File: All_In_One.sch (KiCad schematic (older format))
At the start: 106 parts, among them J1 MS_jumper_xaxis, J10 Motors, J11 Fan, J2 MS_jumper_yaxis, J3 Base_Proxy, J4 Water_Pump, J5 MS_jumper, J6 Stepper_xaxis, J7 Stepper_yaxis, J8 Arm_Proxy, J9 bluetooth, Q1 BC547, U1 Prashant_library_Arduino_Mega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, U10 PC817, U11 PC817, U12 PC817, U13 PC817, U14 5V_Regulator, U15 PC817, U16 PC817, U17 PC817, U2 L298, U3 L298, U4 5V_Regulator, U5 PC817, U6 PC817, U7 PC817, U8 PC817, U9 PC817

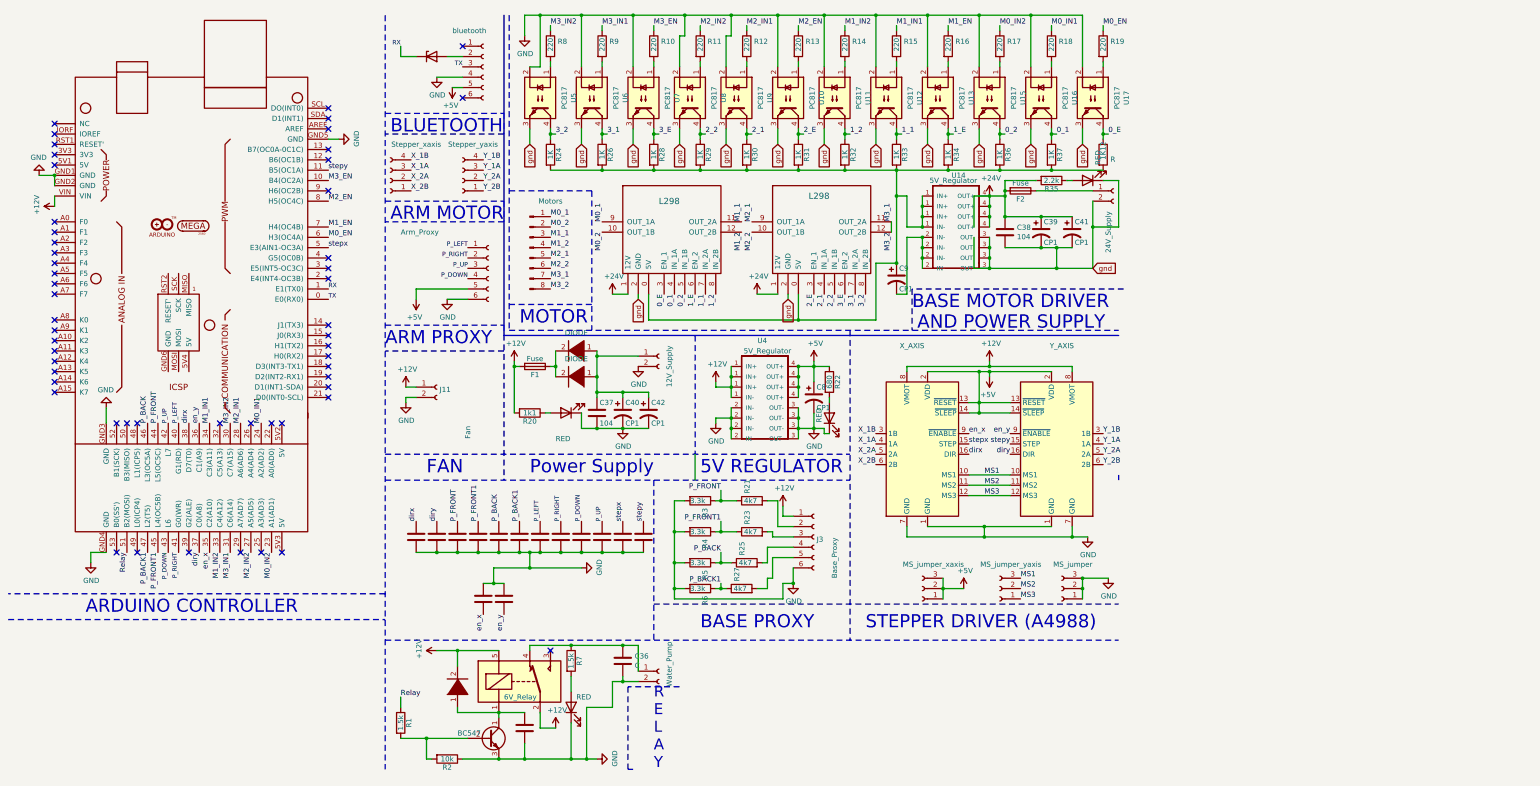
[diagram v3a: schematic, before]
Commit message: completed joining tracks!
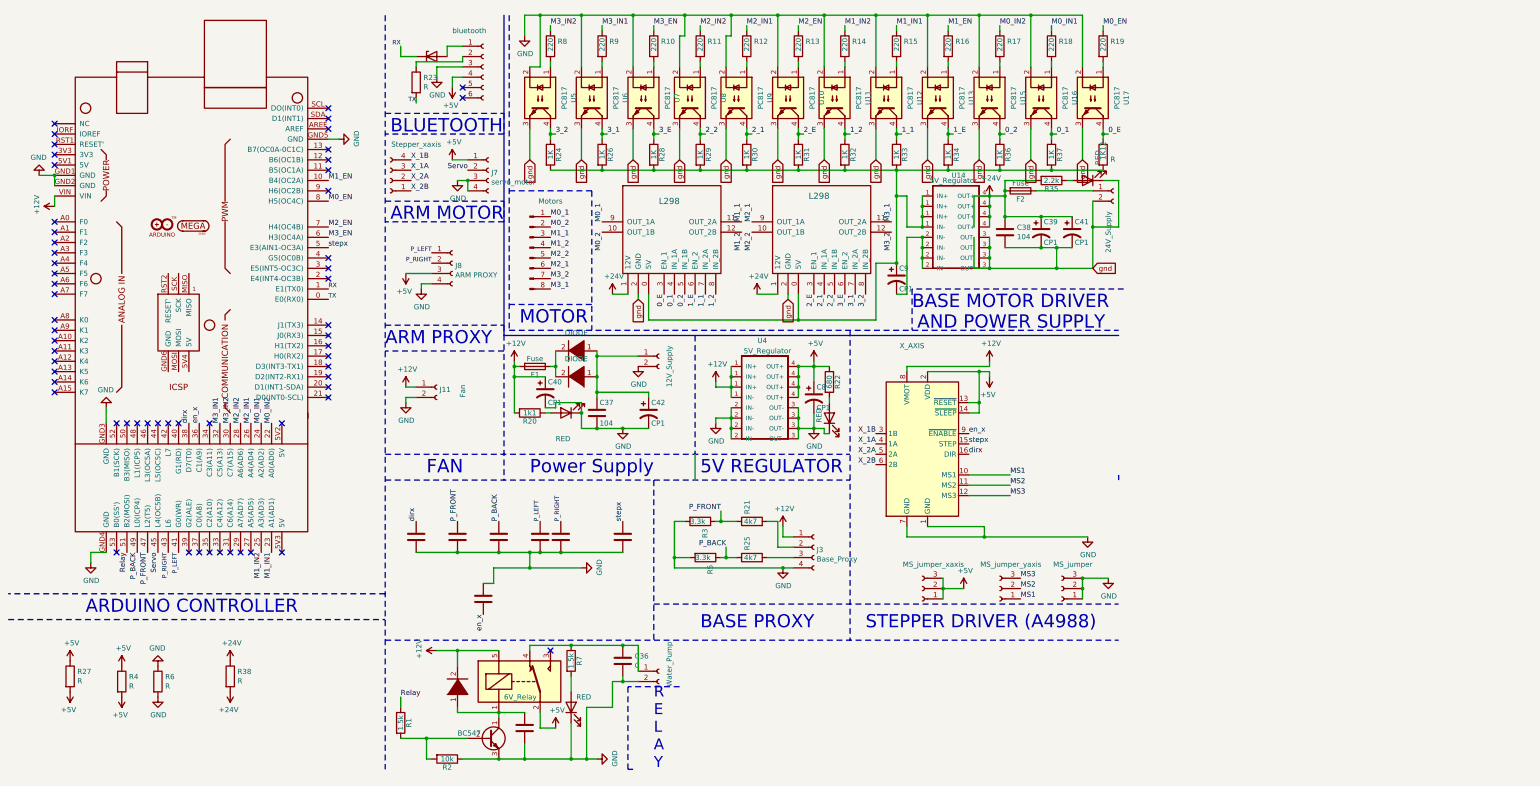
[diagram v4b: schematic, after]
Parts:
- removed A2: Y_AXIS, modFiles:A4998, symbol Driver_Motor:Pololu_Breakout_A4988
- removed C1, C15, C29, C31, C35, C4, C6: C, modFiles:Capacitor_Disc_Small, symbol Device:C
- removed J3: Base_Proxy, 0_18:New_conn_1x6, symbol Connector:Conn_01x06_Female
- removed J8: Arm_Proxy, 0_18:New_conn_1x6, symbol Connector:Conn_01x06_Female
- added J3: Base_Proxy, 0_18:New_conn_1x4, symbol Connector:Conn_01x04_Female
- added J8: ARM PROXY, 0_18:New_conn_1x4, symbol Connector:Conn_01x04_Female
- added R38: R, modFiles:Resistor_small, symbol Device:R
- J7: value Stepper_yaxis -> servo_motor
- R23, R27: value 4k7 -> R
- R4, R6: value 3.3k -> R
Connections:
- net P_DOWN is gone; now on net P_RIGHT: U1.43 (L6)
- net Y_1A is gone; now on net GND: J7.3 (Pin_3)
- net Y_1B is gone; now on net GND: J7.4 (Pin_4)
- net Y_2B is gone; now on net +5V: J7.1 (Pin_1)
- net en_y is gone; now on net en_x: U1.36 (C1(A9))
- net +12V: now also C40.1, J3.1 (Pin_1); no longer Rly1.2
- net +24V: now also R38.1, R38.2
- net +5V: now also J9.4 (Pin_4), R27.1, R27.2, R4.1, R4.2, Rly1.2, J8.3 (Pin_3); no longer J9.5 (Pin_5)
- net GND: now also J9.3 (Pin_3), R6.1, J3.4 (Pin_4), J8.4 (Pin_4); no longer J9.4 (Pin_4), R4.2
- net M0_EN: now also U1.8 (H5(OC4C)); no longer U1.6 (H3(OC4A))
- net M0_IN2: now also U1.22 (A0(AD0)); no longer U1.23 (A1(AD1))
- net M1_EN: now also U1.10 (B4(OC2A)); no longer U1.7 (H4(OC4B))
- net M1_IN1: now also U1.23 (A1(AD1)); no longer U1.34 (C3(A11))
- net M1_IN2: now also U1.25 (A3(AD3)); no longer U1.33 (C4(A12))
- net M2_1: now also J10.6 (Pin_6); no longer J10.5 (Pin_5)
- net M2_2: now also J10.5 (Pin_5); no longer J10.6 (Pin_6)
- net M2_EN: now also U1.7 (H4(OC4B)); no longer U1.8 (H5(OC4C))
- net M2_IN1: now also U1.26 (A4(AD4)); no longer U1.28 (A6(AD6))
- net M2_IN2: now also U1.28 (A6(AD6)); no longer U1.27 (A5(AD5))
- net M3_1: no longer J10.7 (Pin_7), U3.12 (OUT_2B)
- net M3_EN: now also U1.6 (H3(OC4A)); no longer U1.10 (B4(OC2A))
- net M3_IN1: now also U1.32 (C5(A13)); no longer U1.31 (C6(A14))
- net MS1: now also J2.1 (Pin_1); no longer J2.3 (Pin_3)
- net MS3: now also J2.3 (Pin_3); no longer J2.1 (Pin_1)
- net P_BACK: now also U1.49 (L0(ICP4)); no longer U1.46 (L3(OC5A))
- net P_FRONT: now also U1.47 (L2(T5)); no longer U1.44 (L5(OC5C))
- net P_LEFT: now also U1.41 (G0(WR)), J8.1 (Pin_1); no longer U1.40 (G1(RD))
- net P_RIGHT: now also J8.2 (Pin_2); no longer U1.41 (G0(WR))
- net TX: now also R23.2; no longer J9.3 (Pin_3)
- net en_x: no longer U1.35 (C2(A10))
- net at C37.1, C42.1, D10.1 (K)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: no longer C40.1
- net at J9.1 (Pin_1): now also D7.2 (A)
- net at J9.2 (Pin_2): now also R23.1; no longer D7.2 (A)
- net at R21.2: now also J3.2 (Pin_2)
- net at R25.2: now also J3.3 (Pin_3)
- removed net P_BACK1: R27.1, R6.1, U1.47 (L2(T5))
- removed net P_FRONT1: R23.1, R4.1, U1.45 (L4(OC5B))
- net P_UP: no longer names the net of U1.42 (L7)
- net Y_2A renamed Servo
- net Servo: now also U1.45 (L4(OC5B))
- net diry: no longer names the net of U1.37 (C0(A8))
- net stepy: no longer names the net of U1.11 (B5(OC1A))
- new net M3_2: J10.7 (Pin_7), U3.12 (OUT_2B)
- no-connect marks 54 -> 60
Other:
- moved on the sheet: C40, R21, R25, R3, R5

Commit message: completed circuit
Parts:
- J9: footprint modFiles:bluetooth -> 0_18:bluetooth
- R7: value 1.5k -> 470
- U14: footprint modFiles:Buck 5A -> modFiles:Buck_Regulator
- U4: footprint modFiles:Buck_Regulator -> modFiles:Buck_5A
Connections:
- net +24V: now also U14.1 (IN-); no longer U14.4 (OUT+)
- net +5V: now also J9.5 (Pin_5); no longer J9.4 (Pin_4)
- net GND: now also J9.4 (Pin_4); no longer J9.3 (Pin_3)
- net M0_1: now also J10.4 (Pin_4); no longer J10.1 (Pin_1)
- net M0_2: now also J10.3 (Pin_3); no longer J10.2 (Pin_2)
- net M1_1: now also J10.2 (Pin_2); no longer J10.3 (Pin_3)
- net M1_2: now also J10.1 (Pin_1); no longer J10.4 (Pin_4)
- net M3_1: now also J10.7 (Pin_7); no longer J10.8 (Pin_8)
- net M3_2: now also J10.8 (Pin_8); no longer J10.7 (Pin_7)
- net gnd: now also C9.2, U14.2 (IN-)
- net state: now reaches U1.11 (B5(OC1A))
- net state: now also J9.1 (Pin_1)
- net at 1K12.2, C9.1, R24.2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: now also U14.4 (OUT+); no longer U14.1 (IN-)
- net at D7.2 (A): now also J9.2 (Pin_2); no longer J9.1 (Pin_1)
- net at R23.1: now also J9.3 (Pin_3); no longer J9.2 (Pin_2)
- no-connect marks 60 -> 58
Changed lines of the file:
@@
 F 0 "U4" H 7750 3750 50  0000 C CNN
 F 1 "5V_Regulator" H 7800 3650 50  0000 C CNN
-F 2 "modFiles:Buck_Regulator" H 7700 3700 50  0001 C CNN
+F 2 "modFiles:Buck_5A" H 7700 3700 50  0001 C CNN
 F 3 "" H 7700 3700 50  0001 C CNN
 	1    7700 3700
@@
 L power:+24V #PWR022
 U 1 1 5F358F80
-P 9950 2250
-F 0 "#PWR022" H 9950 2100 50  0001 C CNN
-F 1 "+24V" H 9965 2423 50  0000 C CNN
-F 2 "" H 9950 2250 50  0001 C CNN
-F 3 "" H 9950 2250 50  0001 C CNN
-	1    9950 2250
+P 9250 2200
+F 0 "#PWR022" H 9250 2050 50  0001 C CNN
+F 1 "+24V" H 9265 2373 50  0000 C CNN
+F 2 "" H 9250 2200 50  0001 C CNN
+F 3 "" H 9250 2200 50  0001 C CNN
+	1    9250 2200
 	1    0    0    -1
 $EndComp
@@
 F 0 "J9" H 5077 976 50  0001 L CNN
 F 1 "bluetooth" H 4750 1350 50  0000 L CNN
-F 2 "modFiles:bluetooth" H 5050 1000 50  0001 C CNN
+F 2 "0_18:bluetooth" H 5050 1000 50  0001 C CNN
 F 3 "~" H 5050 1000 50  0001 C CNN
 	1    5050 1000
 	1    0    0    -1
 $EndComp
+Text Label 5700 2750 0    50   ~ 0
+M0_1
+Text Label 5700 2650 0    50   ~ 0
+M0_2
+Text Label 5700 2550 0    50   ~ 0
+M1_1
 Text Label 5700 2450 0    50   ~ 0
-M0_1
-Text Label 5700 2550 0    50   ~ 0
-M0_2
-Text Label 5700 2650 0    50   ~ 0
-M1_1
-Text Label 5700 2750 0    50   ~ 0
 M1_2
 Text Label 5700 2950 0    50   ~ 0
@@
 Text Label 5700 2850 0    50   ~ 0
 M2_2
-Text Label 5700 3150 0    50   ~ 0
+Text Label 5700 3050 0    50   ~ 0
 M3_1
 $Comp
@@
 P 5900 6750
 F 0 "R7" V 5980 6750 50  0000 C CNN
-F 1 "1.5k" V 5900 6750 50  0000 C CNN
+F 1 "470" V 5900 6750 50  0000 C CNN
 F 2 "modFiles:Resistor_small" V 5830 6750 50  0001 C CNN
 F 3 "~" H 5900 6750 50  0001 C CNN
@@
 Connection ~ 9050 2000
 Wire Wire Line
-	10100 2200 10100 2250
-Connection ~ 9950 2250
-Wire Wire Line
-	9800 2250 9950 2250
-Wire Wire Line
-	9800 2950 9950 2950
-Wire Wire Line
 	10600 2950 10600 2750
 Connection ~ 9950 2950
 Wire Wire Line
-	9950 2950 10600 2950
+	9950 2950 10250 2950
 Connection ~ 10100 2450
 Connection ~ 10600 2750
@@
 Wire Wire Line
 	7000 500  6500 500
-Wire Wire Line
-	9050 2000 9050 2250
-Wire Wire Line
-	9050 2250 9150 2250
 Text GLabel 10950 2950 2    50   Input ~ 0
 gnd
@@
 	10400 2200 10950 2200
 Wire Wire Line
-	9950 2250 10100 2250
-Wire Wire Line
-	10100 2250 10100 2450
-Connection ~ 10100 2250
-Wire Wire Line
 	6650 3200 6650 3450
 Wire Wire Line
@@
 Connection ~ 9550 2000
 Wire Wire Line
-	9550 2000 10050 2000
+	9550 2000 10000 2000
 $Comp
 L Device:R R36
@@
 Wire Wire Line
 	9050 3200 9150 3200
-Connection ~ 9050 2250
-$Comp
-L BUCK_Controller:BUCK U14
-U 1 1 5F92895C
-P 9550 2050
-F 0 "U14" H 9650 2050 50  0000 C CNN
-F 1 "5V_Regulator" H 9600 2000 50  0000 C CNN
-F 2 "modFiles:Buck 5A" H 9550 2050 50  0001 C CNN
-F 3 "" H 9550 2050 50  0001 C CNN
-	1    9550 2050
-	1    0    0    -1
-$EndComp
-Wire Wire Line
-	9050 2250 9050 2900
 Wire Wire Line
 	9050 2900 8850 2900
@@
 Connection ~ 9050 2900
 Wire Wire Line
-	9150 2250 9150 2550
-Wire Wire Line
-	9800 2650 9800 2950
-Wire Wire Line
-	9800 2250 9800 2550
-Wire Wire Line
 	9150 2650 9150 3200
 Wire Wire Line
-	9300 2250 9300 2350
-Connection ~ 9300 2350
-Wire Wire Line
-	9300 2350 9300 2450
-Connection ~ 9300 2450
-Wire Wire Line
-	9300 2450 9300 2550
-Wire Wire Line
-	9300 2550 9150 2550
-Connection ~ 9300 2550
-Wire Wire Line
-	9300 2650 9300 2750
-Connection ~ 9300 2750
-Wire Wire Line
-	9300 2750 9300 2850
-Connection ~ 9300 2850
-Wire Wire Line
-	9300 2850 9300 2950
-Wire Wire Line
 	9150 2650 9300 2650
-Connection ~ 9300 2650
 Wire Wire Line
 	10700 2100 10750 2100
@@
 	10100 2100 10100 2200
 Connection ~ 10100 2200
-Wire Wire Line
-	9950 2250 9950 2350
-Connection ~ 9950 2350
-Wire Wire Line
-	9950 2350 9950 2450
-Connection ~ 9950 2450
-Wire Wire Line
-	9950 2450 9950 2550
-Wire Wire Line
-	9950 2650 9950 2750
-Connection ~ 9950 2750
-Wire Wire Line
-	9950 2750 9950 2850
-Connection ~ 9950 2850
-Wire Wire Line
-	9950 2850 9950 2950
 Wire Wire Line
 	11050 2100 11200 2100
@@
 	6000 4250 6000 4350
 Connection ~ 6000 4350
-Wire Wire Line
-	4850 800  4700 800
-Wire Wire Line
-	4700 800  4700 900
-Wire Wire Line
-	4850 1000 4600 1000
-Wire Wire Line
-	4600 1000 4600 1100
-Wire Wire Line
-	4850 1100 4750 1100
-Wire Wire Line
-	4750 1100 4750 1200
-NoConn ~ 4850 1200
 NoConn ~ 2600 5700
 NoConn ~ 2800 5700
@@
 	1    0    0    -1
 $EndComp
-Text Label 5700 3050 0    50   ~ 0
+Text Label 5700 3150 0    50   ~ 0
 M3_2
 Wire Wire Line
@@
 Text Label 1900 5700 3    50   ~ 0
 Servo
-NoConn ~ 3550 2000
 $Comp
 L Device:R R23
@@
 	1    0    0    -1
 $EndComp
-Wire Wire Line
-	4850 900  4850 950
-Wire Wire Line
-	4850 950  4400 950
-Wire Wire Line
-	4400 950  4400 1000
 Wire Wire Line
 	4400 1300 4400 1350
@@
 	-1   0    0    1
 $EndComp
+Wire Wire Line
+	9300 3050 10250 3050
+Wire Wire Line
+	10250 3050 10250 2950
+Connection ~ 10250 2950
+Wire Wire Line
+	10250 2950 10600 2950
+Wire Wire Line
+	4750 1200 4850 1200
+Wire Wire Line
+	4850 1100 4600 1100
+Wire Wire Line
+	4850 1000 4400 1000
+Wire Wire Line
+	4850 900  4700 900
+Text Label 4850 800  2    50   ~ 0
+state
+Text Label 3550 2000 0    50   ~ 0
+state
+Wire Wire Line
+	9950 2250 9950 2350
+Connection ~ 9950 2350
+Wire Wire Line
+	9950 2450 9950 2550
+Wire Wire Line
+	9950 2350 9950 2450
+Connection ~ 9950 2450
+Wire Wire Line
+	9950 2650 9950 2750
+Connection ~ 9950 2750
+Wire Wire Line
+	9950 2850 9950 2950
+Wire Wire Line
+	9950 2750 9950 2850
+Connection ~ 9950 2850
+Connection ~ 9300 2650
+Wire Wire Line
+	9300 2650 9300 2750
+Connection ~ 9300 2750
+Wire Wire Line
+	9300 2750 9300 2850
+Connection ~ 9300 2850
+Wire Wire Line
+	9300 2950 9300 3050
+Wire Wire Line
+	9300 2850 9300 2950
+Connection ~ 9300 2950
+Wire Wire Line
+	9300 2250 9300 2350
+Connection ~ 9300 2350
+Wire Wire Line
+	9300 2450 9300 2550
+Wire Wire Line
+	9300 2350 9300 2450
+Connection ~ 9300 2450
+$Comp
+L BUCK_Controller:BUCK U14
+U 1 1 5F92895C
+P 9550 2050
+F 0 "U14" H 9650 2050 50  0000 C CNN
+F 1 "5V_Regulator" H 9600 2000 50  0000 C CNN
+F 2 "modFiles:Buck_Regulator" H 9550 2050 50  0001 C CNN
+F 3 "" H 9550 2050 50  0001 C CNN
+	1    9550 2050
+	1    0    0    -1
+$EndComp
+Wire Wire Line
+	9050 2000 9050 2900
+Wire Wire Line
+	10100 2200 10100 2450
+Connection ~ 9300 2250
+Wire Wire Line
+	9250 2200 9250 2250
+Wire Wire Line
+	9250 2250 9300 2250
+Wire Wire Line
+	9950 2350 10000 2350
+Wire Wire Line
+	10000 2350 10000 2000
+Connection ~ 10000 2000
+Wire Wire Line
+	10000 2000 10050 2000
+Wire Wire Line
+	10100 2200 10050 2200
+Wire Wire Line
+	10050 2200 10050 2600
+Wire Wire Line
+	10050 2600 9250 2600
+Wire Wire Line
+	9250 2600 9250 2250
+Connection ~ 9250 2250
 $EndSCHEMATC

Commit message: completed circuit1
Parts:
- added C1: CP1, modFiles:Capacitor_1000uF, symbol Device:CP1
- added R39, R40: R, modFiles:Resistor_small, symbol Device:R
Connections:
- net +12V: now also C1.1
- net GND: now also C1.2
- net M3_1: now also R39.1, R39.2
- net M3_2: now also R40.1, R40.2
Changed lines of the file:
@@
 L power:+12V #PWR01
 U 1 1 5F3623D7
-P 900 2350
-F 0 "#PWR01" H 900 2200 50  0001 C CNN
-F 1 "+12V" H 915 2523 50  0000 C CNN
-F 2 "" H 900 2350 50  0001 C CNN
-F 3 "" H 900 2350 50  0001 C CNN
-	1    900  2350
+P 750 2200
+F 0 "#PWR01" H 750 2050 50  0001 C CNN
+F 1 "+12V" H 765 2373 50  0000 C CNN
+F 2 "" H 750 2200 50  0001 C CNN
+F 3 "" H 750 2200 50  0001 C CNN
+	1    750  2200
 	0    -1   -1   0
 $EndComp
@@
 	9250 2600 9250 2250
 Connection ~ 9250 2250
+$Comp
+L Device:R R39
+U 1 1 5F3BBC85
+P 3350 6950
+F 0 "R39" H 3420 6996 50  0000 L CNN
+F 1 "R" H 3420 6905 50  0000 L CNN
+F 2 "modFiles:Resistor_small" V 3280 6950 50  0001 C CNN
+F 3 "~" H 3350 6950 50  0001 C CNN
+	1    3350 6950
+	1    0    0    -1
+$EndComp
+Text Label 3350 6800 1    50   ~ 0
+M3_1
+Text Label 3350 7100 3    50   ~ 0
+M3_1
+$Comp
+L Device:R R40
+U 1 1 5F3BC3AD
+P 3750 6950
+F 0 "R40" H 3820 6996 50  0000 L CNN
+F 1 "R" H 3820 6905 50  0000 L CNN
+F 2 "modFiles:Resistor_small" V 3680 6950 50  0001 C CNN
+F 3 "~" H 3750 6950 50  0001 C CNN
+	1    3750 6950
+	1    0    0    -1
+$EndComp
+Text Label 3750 6800 1    50   ~ 0
+M3_2
+Text Label 3750 7100 3    50   ~ 0
+M3_2
+$Comp
+L Device:CP1 C1
+U 1 1 5F3BCF50
+P 650 2550
+F 0 "C1" H 675 2650 50  0000 L CNN
+F 1 "CP1" H 675 2450 50  0000 L CNN
+F 2 "modFiles:Capacitor_1000uF" H 650 2550 50  0001 C CNN
+F 3 "~" H 650 2550 50  0001 C CNN
+	1    650  2550
+	1    0    0    -1
+$EndComp
+Wire Wire Line
+	650  2400 650  2350
+Wire Wire Line
+	650  2350 900  2350
+Wire Wire Line
+	750  2200 900  2200
+Wire Wire Line
+	900  2200 900  2250
+Connection ~ 900  2250
+$Comp
+L power:GND #PWR041
+U 1 1 5F3F976C
+P 650 2700
+F 0 "#PWR041" H 650 2450 50  0001 C CNN
+F 1 "GND" H 655 2527 50  0000 C CNN
+F 2 "" H 650 2700 50  0001 C CNN
+F 3 "" H 650 2700 50  0001 C CNN
+	1    650  2700
+	1    0    0    -1
+$EndComp
 $EndSCHEMATC
